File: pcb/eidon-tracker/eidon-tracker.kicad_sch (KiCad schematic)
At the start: 3 parts, among them SW1 SS-12D00-G 4 E, U1 XIAO-ESP32C6, U2 GY-BNO085

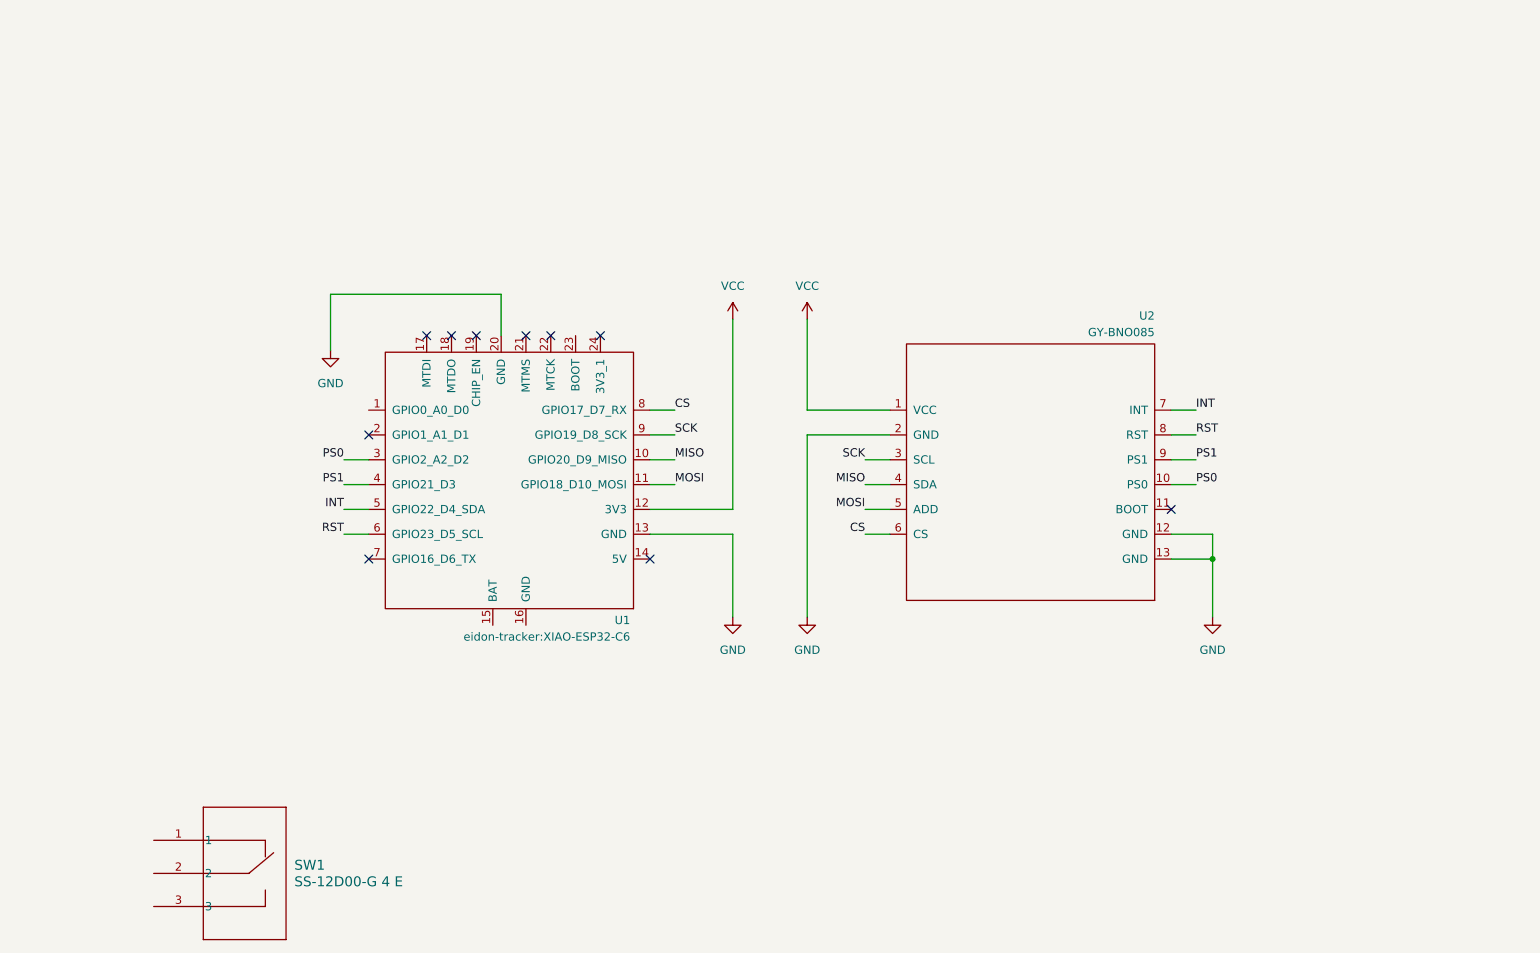
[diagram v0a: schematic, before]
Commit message: feat(pcb): implements battery connector and power switch toggle
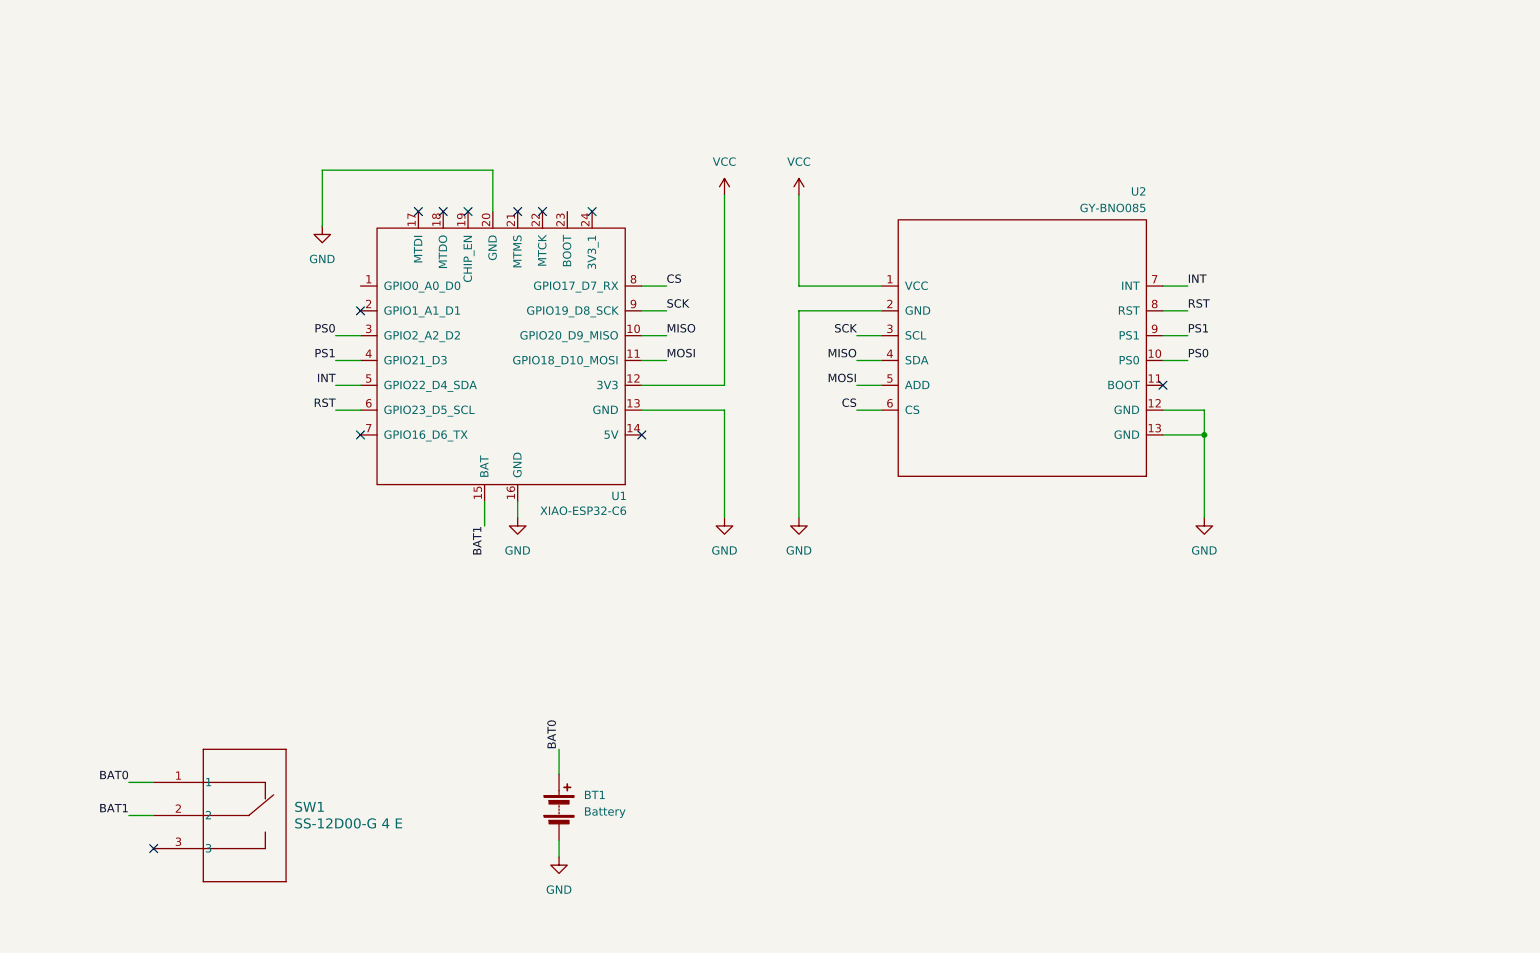
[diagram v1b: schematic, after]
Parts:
- added BT1: Battery, Connector_JST:JST_PH_S2B-PH-K_1x02_P2.00mm_Horizontal, symbol Device:Battery
- U1: footprint eidon-tracker:XIAO-ESP32-C6 -> XIAO-ESP32-C6
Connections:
- net GND: now also U1.16 (GND), BT1.2 (-)
- net BAT1: now reaches U1.15 (BAT)
- net BAT1: now also SW1.2
- net BAT0: now reaches SW1.1
- net BAT0: now also BT1.1 (+)
- no-connect marks 10 -> 11
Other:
- moved on the sheet: SW1, U1, U2

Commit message: feat(pcb): implements battery charging circuit and optimizes esp32-c6 footprint for what is needed
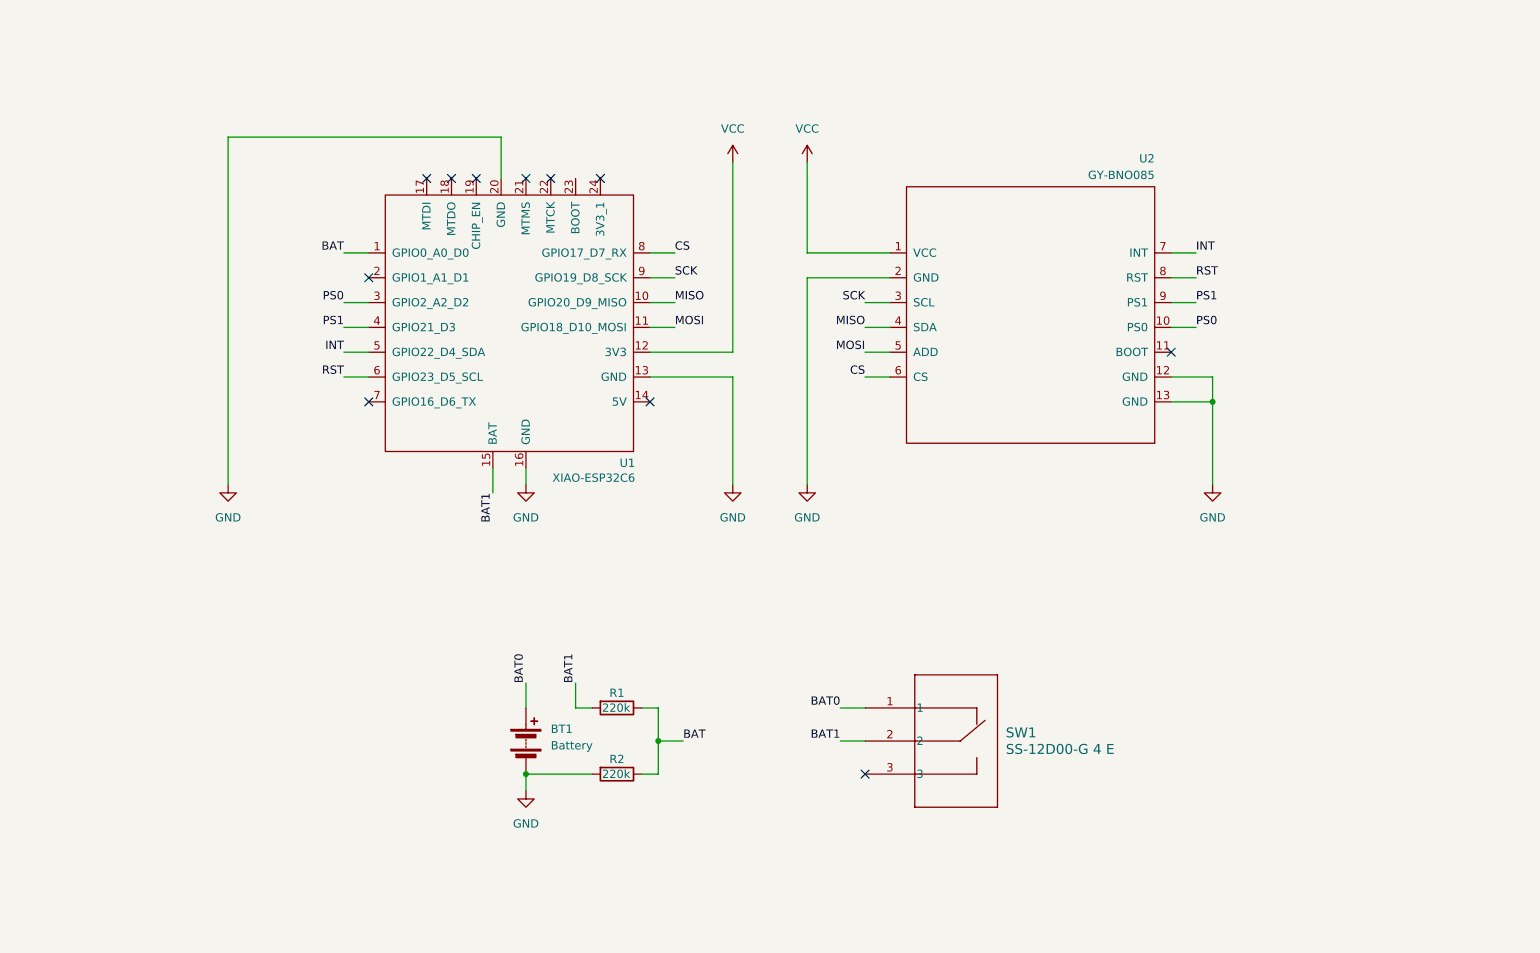
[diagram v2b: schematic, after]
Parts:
- added R1, R2: 220k, Resistor_SMD:R_0805_2012Metric, symbol Device:R
- U1: footprint XIAO-ESP32-C6 -> XIAO-ESP32C6
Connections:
- net BAT1: now also R1.2
- net GND: now also R2.2
- net BAT: now reaches U1.1 (GPIO0_A0_D0)
- net BAT: now also R1.1, R2.1
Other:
- moved on the sheet: BT1, SW1, U1, U2

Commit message: feat(pcb): further optimizations to PCB layout and implements boot/user button
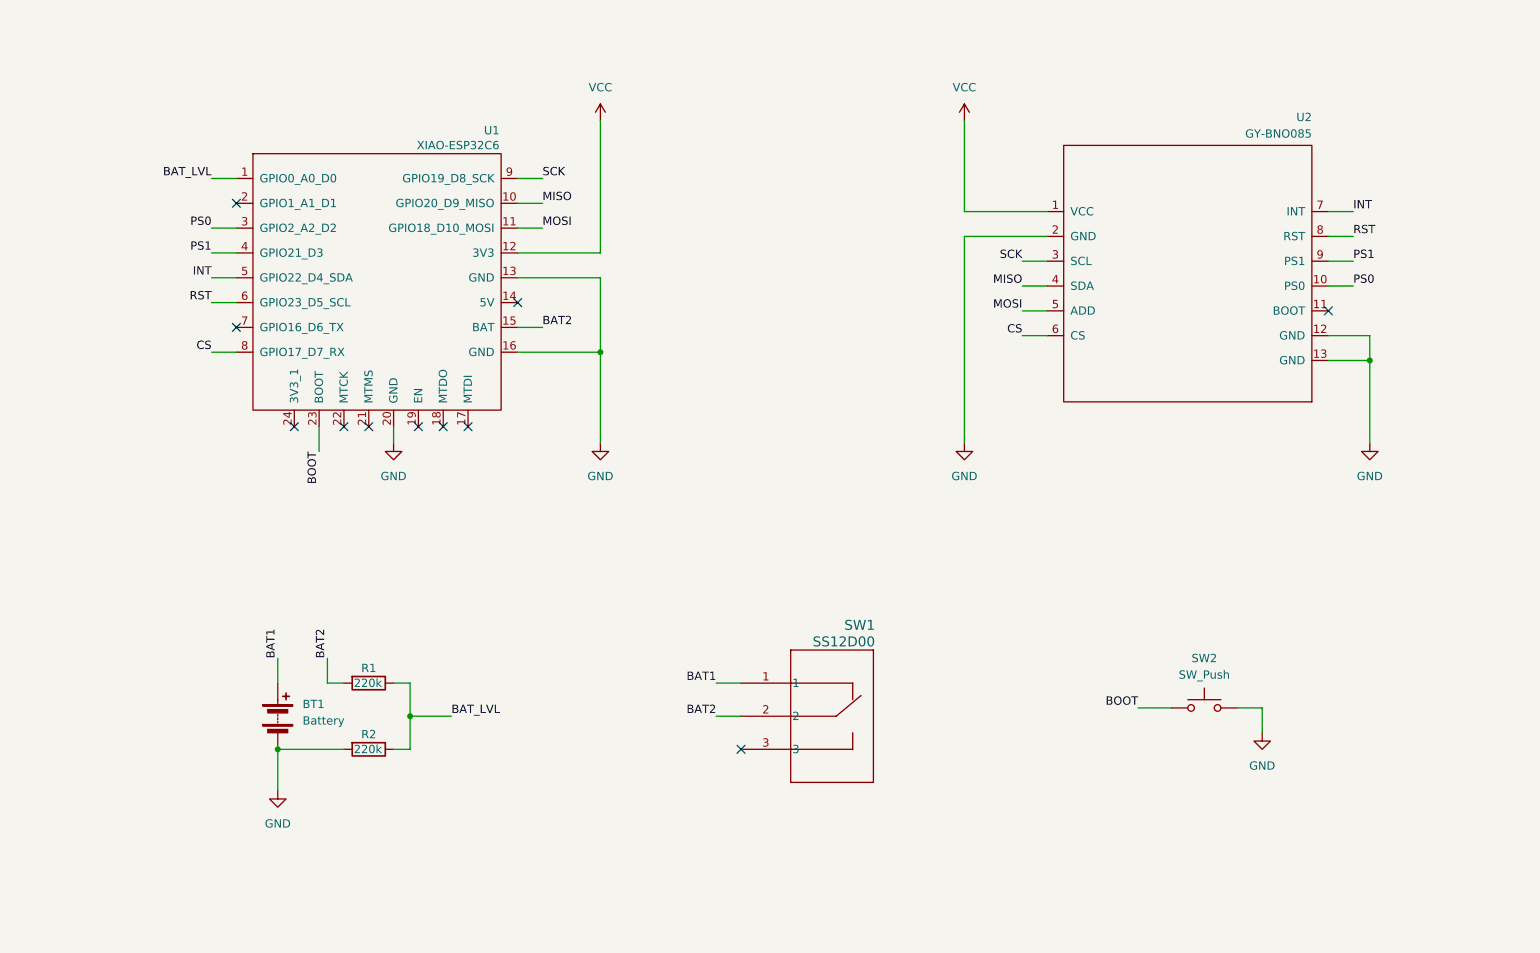
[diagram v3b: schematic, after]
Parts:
- added SW2: SW_Push, Button_Switch_SMD:SW_Push_SPST_NO_Alps_SKRK, symbol Switch:SW_Push
- SW1: value SS-12D00-G 4 E -> SS12D00
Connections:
- net BAT0 is gone; now on net BAT1: BT1.1 (+), SW1.1
- net BAT1: no longer R1.2, SW1.2, U1.15 (BAT)
- net GND: now also SW2.2
- net BOOT: now reaches U1.23 (BOOT)
- net BOOT: now also SW2.1
- net BAT renamed BAT_LVL
- new net BAT2: R1.2, SW1.2, U1.15 (BAT)
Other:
- moved on the sheet: BT1, R1, R2, SW1, U1, U2

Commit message: feat(pcb): implements button and led circuit with smd componenets; chore(pcb): cleans up schematic and adds group labels to make the parts easier to understand
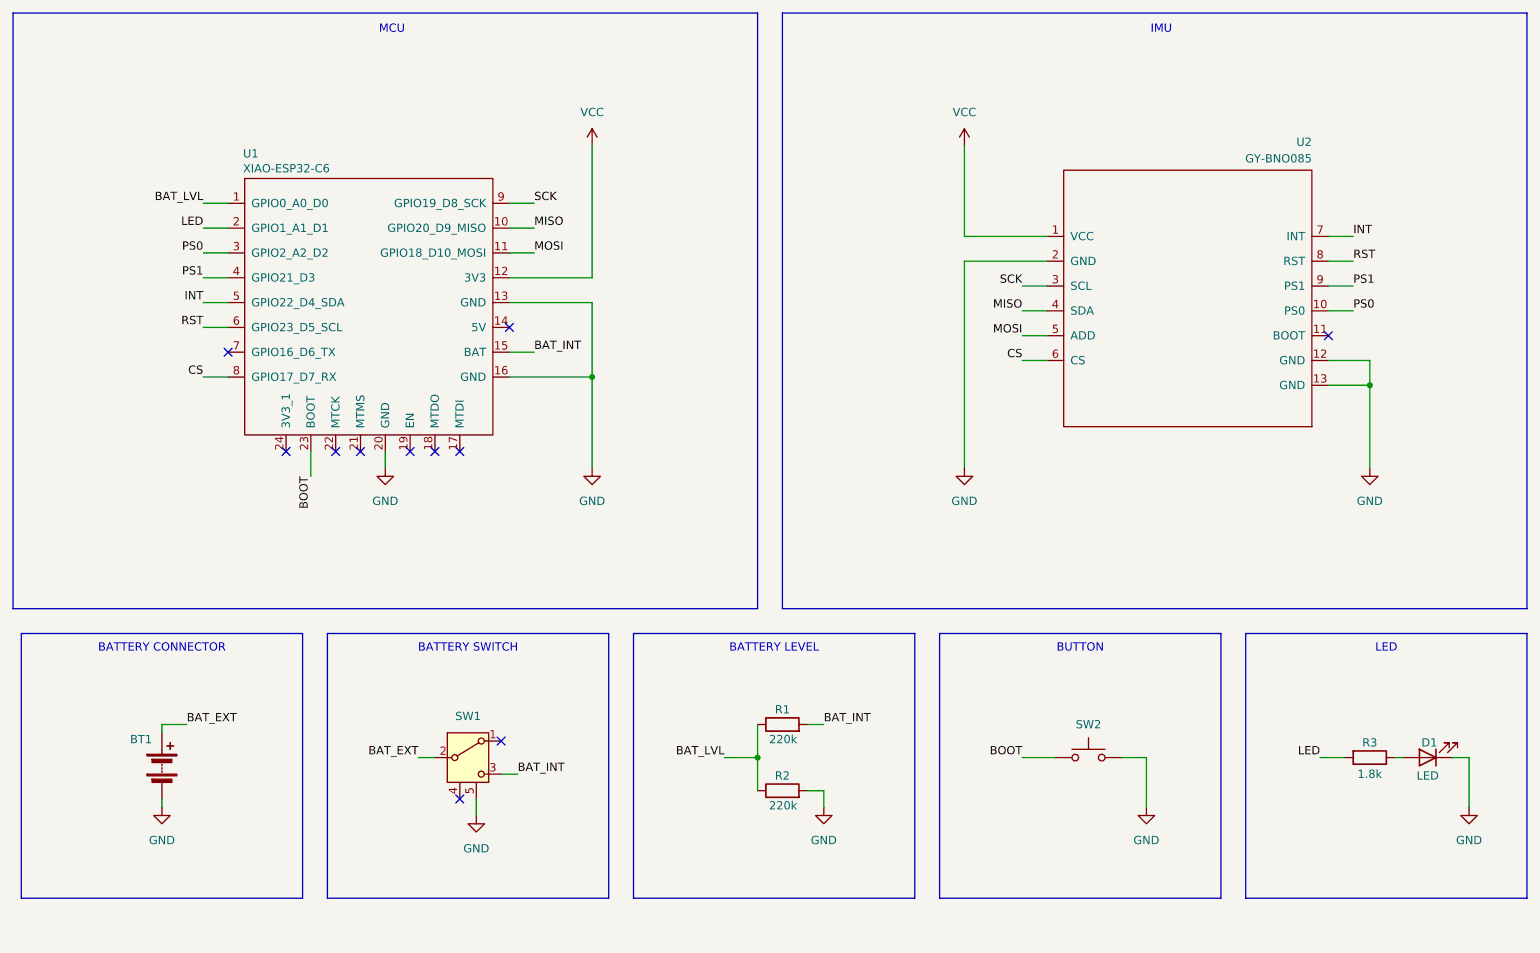
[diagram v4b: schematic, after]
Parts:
- removed SW1: SS12D00, 1P2T_SS-12D00_CNK, symbol eidon-tracker:SS-12D00-G_4_E
- added D1: LED, LED_SMD:LED_0805_2012Metric, symbol Device:LED
- added R3: 1.8k, Resistor_SMD:R_0805_2012Metric, symbol Device:R
- added SW1: SW_SPDT, Button_Switch_THT:SW_Slide_SPDT_Angled_CK_OS102011MA1Q, symbol eidon-tracker:SW_SPDT
- U1: footprint XIAO-ESP32C6 -> XIAO-ESP32-C6
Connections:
- net GND: now also D1.1 (K), SW1.5 (S)
- net LED: now reaches U1.2 (GPIO1_A1_D1)
- net LED: now also R3.2
- net BAT1 renamed BAT_EXT
- net BAT_EXT: now also SW1.2 (B)
- net BAT2 renamed BAT_INT
- net BAT_INT: now also SW1.3 (C)
- new net: D1.2 (A), R3.1
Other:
- note added: "BATTERY CONNECTOR"
- note added: "BATTERY LEVEL"
- note added: "BATTERY SWITCH"
- note added: "BUTTON"
- note added: "IMU"
- note added: "LED"
- note added: "MCU"
- moved on the sheet: BT1, R1, R2, SW2, U1, U2
